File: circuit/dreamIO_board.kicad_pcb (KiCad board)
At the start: 2 copper layers, 60 x 60 mm, 77 parts, among them IC1 TPS61200, P1 BATT, P2 CONN_01X08, P3 CONN_01X08, P4 CONN_01X02, P5 CONN_01X06, P6 gnd_con, P7 CONN_01X03, P9 PixelOut, SW1 SPDT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

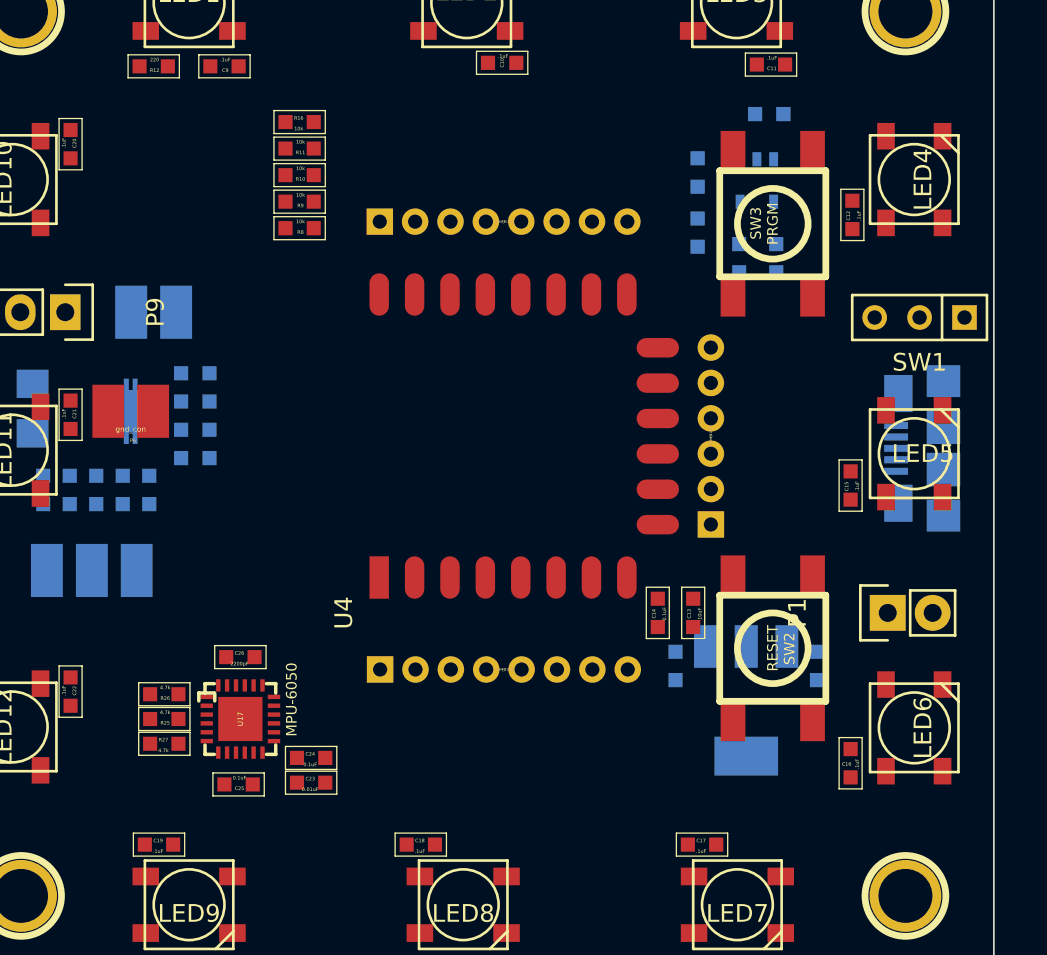
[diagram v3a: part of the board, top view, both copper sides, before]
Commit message: added human input buttons
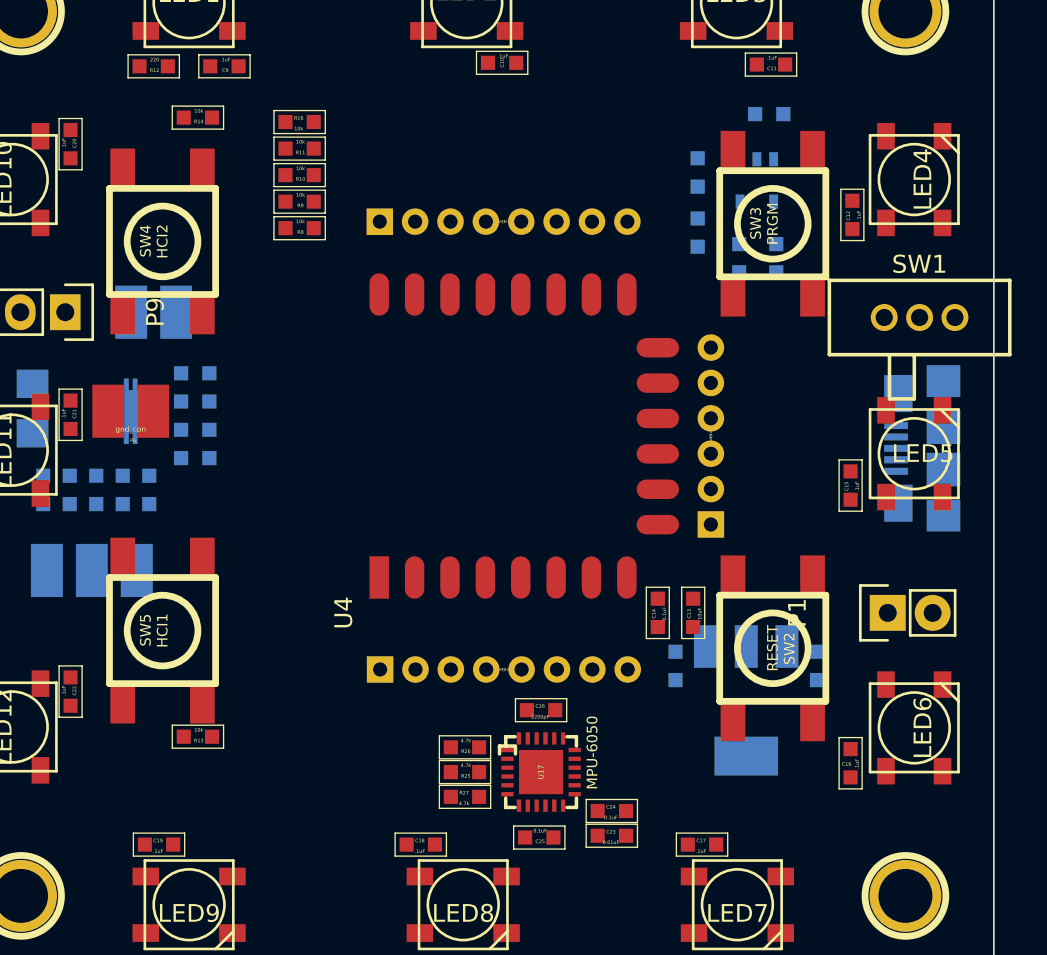
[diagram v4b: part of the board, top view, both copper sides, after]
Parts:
- added R13: 10k, kicad-libraries:0603, F.Cu at (29.3, 59.7)
- added R14: 10k, kicad-libraries:0603, F.Cu at (29.3, 24.7)
- added SW4: HCI2, kicad-libraries:SW_06_SMD, F.Cu at (27.3, 31.7)
- added SW5: HCI1, kicad-libraries:SW_06_SMD, F.Cu at (27.3, 53.7)
- SW1: footprint Buttons_Switches_ThroughHole:SW_Micro_SPST -> dpst:DPST_TE_SSJ12R04
- moved C25 17.3 mm to (48.6, 65.4)
- moved C26 17.3 mm to (48.7, 58.2)
- moved U17 17.3 mm to (48.7, 61.7)
- moved C23 17.3 mm to (52.7, 65.3)
- moved C24 17.3 mm to (52.7, 63.9)
- moved R25 17.3 mm to (44.4, 61.7)
- moved R26 17.3 mm to (44.4, 60.3)
- moved R27 17.3 mm to (44.4, 63.1)
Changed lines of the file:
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@@
 (kicad_pcb (version 4) (host pcbnew 4.0.2-stable)
   (general
-    (links 187)
-    (no_connects 187)
+    (links 199)
+    (no_connects 199)
     (area 14.249999 13.649999 74.350001 73.750001)
     (thickness 1.6)
@@
     (tracks 0)
     (zones 0)
-    (modules 77)
+    (modules 81)
     (nets 53)
   )
@@
   )
   (module kicad-libraries:0603 locked (layer F.Cu)
-    (at 35.7 62.3 180)
+    (at 52.7 65.3 180)
     (attr smd)
     (fp_text reference C23 (at 0.05 0.225 180) (layer F.SilkS)
@@
   )
   (module kicad-libraries:0603 (layer F.Cu)
-    (at 35.7 60.9 180)
+    (at 52.7 63.9 180)
     (attr smd)
     (fp_text reference C24 (at 0.05 0.225 180) (layer F.SilkS)
@@
   )
   (module kicad-libraries:0603 locked (layer F.Cu)
-    (at 31.6 62.4)
+    (at 48.6 65.4)
     (attr smd)
     (fp_text reference C25 (at 0.05 0.225) (layer F.SilkS)
@@
   )
   (module kicad-libraries:0603 locked (layer F.Cu)
-    (at 31.7 55.2 180)
+    (at 48.7 58.2 180)
     (attr smd)
     (fp_text reference C26 (at 0.05 0.225 180) (layer F.SilkS)
@@
   )
   (module kicad-libraries:0603 locked (layer F.Cu)
-    (at 27.4 58.7)
+    (at 44.4 61.7)
     (attr smd)
     (fp_text reference R25 (at 0.05 0.225) (layer F.SilkS)
@@
   )
   (module kicad-libraries:0603 locked (layer F.Cu)
-    (at 27.4 57.3)
+    (at 44.4 60.3)
     (attr smd)
     (fp_text reference R26 (at 0.05 0.225) (layer F.SilkS)
@@
   )
   (module kicad-libraries:0603 locked (layer F.Cu)
-    (at 27.4 60.1 180)
+    (at 44.4 63.1 180)
     (attr smd)
     (fp_text reference R27 (at 0.05 0.225 180) (layer F.SilkS)
@@
     (pad 2 smd rect (at 0.8001 0 180) (size 0.8001 0.8001) (layers F.Cu F.Paste F.Mask)
       (net 2 GND))
-  )
-  (module Buttons_Switches_ThroughHole:SW_Micro_SPST (layer F.Cu)
-    (at 70.1 36 180)
-    (tags "Switch Micro SPST")
-    (fp_text reference SW1 (at 0 -2.54 180) (layer F.SilkS)
-      (effects (font (size 1 1) (thickness 0.15)))
-    )
-    (fp_text value SPDT (at 0.025 2.45 180) (layer F.Fab)
-      (effects (font (size 1 1) (thickness 0.15)))
-    )
-    (fp_line (start -3.81 1.27) (end -3.81 -1.27) (layer F.SilkS) (width 0.15))
-    (fp_line (start -3.81 -1.27) (end 3.81 -1.27) (layer F.SilkS) (width 0.15))
-    (fp_line (start 3.81 -1.27) (end 3.81 1.27) (layer F.SilkS) (width 0.15))
-    (fp_line (start 3.81 1.27) (end -3.81 1.27) (layer F.SilkS) (width 0.15))
-    (fp_line (start -1.27 -1.27) (end -1.27 1.27) (layer F.SilkS) (width 0.15))
-    (pad 1 thru_hole rect (at -2.54 0 180) (size 1.397 1.397) (drill 0.8128) (layers *.Cu *.Mask F.SilkS)
-      (net 4 "Net-(C3-Pad1)"))
-    (pad 2 thru_hole circle (at 0 0 180) (size 1.397 1.397) (drill 0.8128) (layers *.Cu *.Mask F.SilkS)
-      (net 3 +BATT))
-    (pad 3 thru_hole circle (at 2.54 0 180) (size 1.397 1.397) (drill 0.8128) (layers *.Cu *.Mask F.SilkS))
-    (model Buttons_Switches_ThroughHole.3dshapes/SW_Micro_SPST.wrl
-      (at (xyz 0 0 0))
-      (scale (xyz 0.33 0.33 0.33))
-      (rotate (xyz 0 0 0))
-    )
   )
   (module kicad-libraries:SOT23-5 (layer B.Cu)
@@
   )
   (module kicad-libraries:QFN-24-4x4-EP locked (layer F.Cu)
-    (at 31.7 58.7 270)
+    (at 48.7 61.7 270)
     (fp_text reference U17 (at 0 0 270) (layer F.SilkS)
       (effects (font (size 0.29972 0.29972) (thickness 0.06096)))
@@
     (pad 1 thru_hole circle (at 0 0) (size 4.064 4.064) (drill 3.048) (layers *.Cu *.Mask F.SilkS))
   )
+  (module kicad-libraries:0603 (layer F.Cu)
+    (at 29.3 59.7)
+    (attr smd)
+    (fp_text reference R13 (at 0.05 0.225) (layer F.SilkS)
+      (effects (font (size 0.2 0.2) (thickness 0.05)))
+    )
+    (fp_text value 10k (at 0.05 -0.375) (layer F.SilkS)
+      (effects (font (size 0.2 0.2) (thickness 0.05)))
+    )
+    (fp_line (start -1.45034 -0.65024) (end 1.45034 -0.65024) (layer F.SilkS) (width 0.001))
+    (fp_line (start 1.45034 -0.65024) (end 1.45034 0.65024) (layer F.SilkS) (width 0.001))
+    (fp_line (start 1.45034 0.65024) (end -1.45034 0.65024) (layer F.SilkS) (width 0.001))
+    (fp_line (start -1.45034 0.65024) (end -1.45034 -0.65024) (layer F.SilkS) (width 0.001))
+    (pad 1 smd rect (at -0.8001 0) (size 0.8001 0.8001) (layers F.Cu F.Paste F.Mask)
+      (net 2 GND))
+    (pad 2 smd rect (at 0.8001 0) (size 0.8001 0.8001) (layers F.Cu F.Paste F.Mask)
+      (net 9 +3V3))
+  )
+  (module kicad-libraries:0603 (layer F.Cu)
+    (at 29.3 24.7)
+    (attr smd)
+    (fp_text reference R14 (at 0.05 0.225) (layer F.SilkS)
+      (effects (font (size 0.2 0.2) (thickness 0.05)))
+    )
+    (fp_text value 10k (at 0.05 -0.375) (layer F.SilkS)
+      (effects (font (size 0.2 0.2) (thickness 0.05)))
+    )
+    (fp_line (start -1.45034 -0.65024) (end 1.45034 -0.65024) (layer F.SilkS) (width 0.001))
+    (fp_line (start 1.45034 -0.65024) (end 1.45034 0.65024) (layer F.SilkS) (width 0.001))
+    (fp_line (start 1.45034 0.65024) (end -1.45034 0.65024) (layer F.SilkS) (width 0.001))
+    (fp_line (start -1.45034 0.65024) (end -1.45034 -0.65024) (layer F.SilkS) (width 0.001))
+    (pad 1 smd rect (at -0.8001 0) (size 0.8001 0.8001) (layers F.Cu F.Paste F.Mask)
+      (net 2 GND))
+    (pad 2 smd rect (at 0.8001 0) (size 0.8001 0.8001) (layers F.Cu F.Paste F.Mask)
+      (net 9 +3V3))
+  )
+  (module dpst:DPST_TE_SSJ12R04 (layer F.Cu)
+    (at 70.1 36 180)
+    (fp_text reference SW1 (at 0 3 180) (layer F.SilkS)
+      (effects (font (size 1.016 1.016) (thickness 0.1524)))
+    )
+    (fp_text value SPDT (at 0 -5.4 180) (layer F.SilkS) hide
+      (effects (font (size 1.016 1.016) (thickness 0.1524)))
+    )
+    (fp_line (start 1.69926 -2.10058) (end 1.69926 -4.59994) (layer F.SilkS) (width 0.20066))
+    (fp_line (start 1.69926 -4.59994) (end 0.29972 -4.59994) (layer F.SilkS) (width 0.20066))
+    (fp_line (start 0.29972 -4.59994) (end 0.29972 -2.10058) (layer F.SilkS) (width 0.20066))
+    (fp_line (start 5.10032 -2.10058) (end -5.10032 -2.10058) (layer F.SilkS) (width 0.20066))
+    (fp_line (start -5.10032 -2.10058) (end -5.10032 2.10058) (layer F.SilkS) (width 0.20066))
+    (fp_line (start -5.10032 2.10058) (end 5.10032 2.10058) (layer F.SilkS) (width 0.20066))
+    (fp_line (start 5.10032 2.10058) (end 5.10032 -2.10058) (layer F.SilkS) (width 0.20066))
+    (pad 1 thru_hole circle (at -1.99898 0 180) (size 1.524 1.524) (drill 0.97028) (layers *.Cu *.Mask F.SilkS)
+      (net 4 "Net-(C3-Pad1)"))
+    (pad 2 thru_hole circle (at 0 0 180) (size 1.524 1.524) (drill 0.97028) (layers *.Cu *.Mask F.SilkS)
+      (net 3 +BATT))
+    (pad 3 thru_hole circle (at 1.99898 0 180) (size 1.524 1.524) (drill 0.97028) (layers *.Cu *.Mask F.SilkS))
+    (model 3D/Switches/TE_SSJ12R04.wrl
+      (at (xyz 0 0 0))
+      (scale (xyz 0.3937 0.3937 0.3937))
+      (rotate (xyz 0 0 0))
+    )
+  )
+  (module kicad-libraries:SW_06_SMD (layer F.Cu)
+    (at 27.3 31.7 90)
+    (fp_text reference SW4 (at 0.0254 -0.94996 90) (layer F.SilkS)
+      (effects (font (size 0.59944 0.59944) (thickness 0.09906)))
+    )
+    (fp_text value HCI2 (at 0 0 90) (layer F.SilkS)
+      (effects (font (size 0.59944 0.59944) (thickness 0.09906)))
+    )
+    (fp_circle (center 0 0) (end 1.99898 0) (layer F.SilkS) (width 0.381))
+    (fp_line (start -2.99974 -2.99974) (end 2.99974 -2.99974) (layer F.SilkS) (width 0.381))
+    (fp_line (start 2.99974 -2.99974) (end 2.99974 2.99974) (layer F.SilkS) (width 0.381))
+    (fp_line (start 2.99974 2.99974) (end -2.99974 2.99974) (layer F.SilkS) (width 0.381))
+    (fp_line (start -2.99974 2.99974) (end -2.99974 -2.99974) (layer F.SilkS) (width 0.381))
+    (pad 1 smd rect (at -4.20116 -2.25044 90) (size 2.10058 1.39954) (layers F.Cu F.Paste F.Mask)
+      (net 35 GPIO16))
+    (pad 2 smd rect (at -4.20116 2.25044 90) (size 2.10058 1.39954) (layers F.Cu F.Paste F.Mask)
+      (net 9 +3V3))
+    (pad 2 smd rect (at 4.20116 2.25044 90) (size 2.10058 1.39954) (layers F.Cu F.Paste F.Mask)
+      (net 9 +3V3))
+    (pad 1 smd rect (at 4.20116 -2.25044 90) (size 2.10058 1.39954) (layers F.Cu F.Paste F.Mask)
+      (net 35 GPIO16))
+  )
+  (module kicad-libraries:SW_06_SMD (layer F.Cu)
+    (at 27.3 53.7 90)
+    (fp_text reference SW5 (at 0.0254 -0.94996 90) (layer F.SilkS)
+      (effects (font (size 0.59944 0.59944) (thickness 0.09906)))
+    )
+    (fp_text value HCI1 (at 0 0 90) (layer F.SilkS)
+      (effects (font (size 0.59944 0.59944) (thickness 0.09906)))
+    )
+    (fp_circle (center 0 0) (end 1.99898 0) (layer F.SilkS) (width 0.381))
+    (fp_line (start -2.99974 -2.99974) (end 2.99974 -2.99974) (layer F.SilkS) (width 0.381))
+    (fp_line (start 2.99974 -2.99974) (end 2.99974 2.99974) (layer F.SilkS) (width 0.381))
+    (fp_line (start 2.99974 2.99974) (end -2.99974 2.99974) (layer F.SilkS) (width 0.381))
+    (fp_line (start -2.99974 2.99974) (end -2.99974 -2.99974) (layer F.SilkS) (width 0.381))
+    (pad 1 smd rect (at -4.20116 -2.25044 90) (size 2.10058 1.39954) (layers F.Cu F.Paste F.Mask)
+      (net 37 GPIO14))
+    (pad 2 smd rect (at -4.20116 2.25044 90) (size 2.10058 1.39954) (layers F.Cu F.Paste F.Mask)
+      (net 9 +3V3))
+    (pad 2 smd rect (at 4.20116 2.25044 90) (size 2.10058 1.39954) (layers F.Cu F.Paste F.Mask)
+      (net 9 +3V3))
+    (pad 1 smd rect (at 4.20116 -2.25044 90) (size 2.10058 1.39954) (layers F.Cu F.Paste F.Mask)
+      (net 37 GPIO14))
+  )
   (gr_line (start 14.3 13.7) (end 24.3 13.7) (angle 90) (layer Cmts.User) (width 0.2))

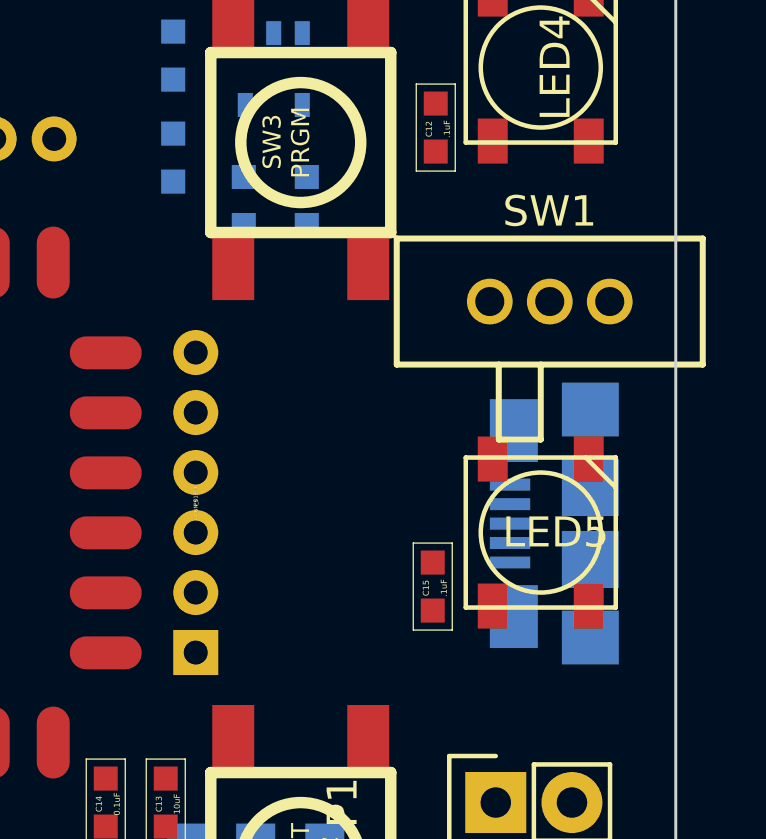
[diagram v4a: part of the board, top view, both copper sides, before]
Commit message: moved the on off switch
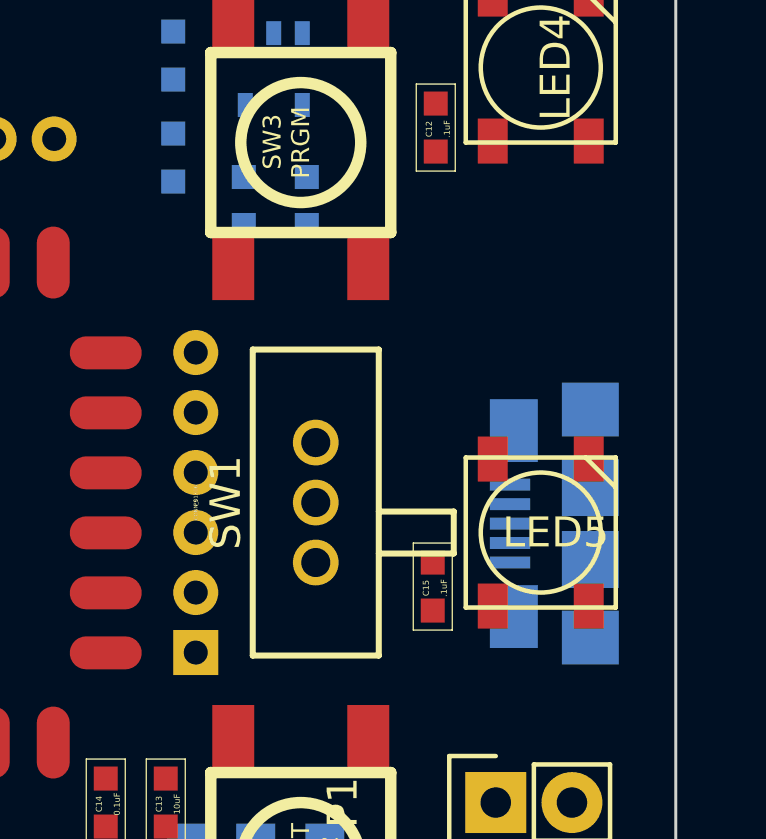
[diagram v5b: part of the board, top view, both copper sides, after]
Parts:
- moved SW1 10.3 mm to (62.3, 42.7), turned to 270 degrees
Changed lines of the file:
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@@
     (links 199)
     (no_connects 199)
-    (area 14.249999 13.649999 74.350001 73.750001)
+    (area 14.199999 13.599999 75.500651 73.750001)
     (thickness 1.6)
     (drawings 8)
@@
   )
   (module dpst:DPST_TE_SSJ12R04 (layer F.Cu)
-    (at 70.1 36 180)
-    (fp_text reference SW1 (at 0 3 180) (layer F.SilkS)
+    (at 62.3 42.7 270)
+    (fp_text reference SW1 (at 0 3 270) (layer F.SilkS)
       (effects (font (size 1.016 1.016) (thickness 0.1524)))
     )
-    (fp_text value SPDT (at 0 -5.4 180) (layer F.SilkS) hide
+    (fp_text value SPDT (at 0 -5.4 270) (layer F.SilkS) hide
       (effects (font (size 1.016 1.016) (thickness 0.1524)))
     )
@@
     (fp_line (start -5.10032 2.10058) (end 5.10032 2.10058) (layer F.SilkS) (width 0.20066))
     (fp_line (start 5.10032 2.10058) (end 5.10032 -2.10058) (layer F.SilkS) (width 0.20066))
-    (pad 1 thru_hole circle (at -1.99898 0 180) (size 1.524 1.524) (drill 0.97028) (layers *.Cu *.Mask F.SilkS)
+    (pad 1 thru_hole circle (at -1.99898 0 270) (size 1.524 1.524) (drill 0.97028) (layers *.Cu *.Mask F.SilkS)
       (net 4 "Net-(C3-Pad1)"))
-    (pad 2 thru_hole circle (at 0 0 180) (size 1.524 1.524) (drill 0.97028) (layers *.Cu *.Mask F.SilkS)
+    (pad 2 thru_hole circle (at 0 0 270) (size 1.524 1.524) (drill 0.97028) (layers *.Cu *.Mask F.SilkS)
       (net 3 +BATT))
-    (pad 3 thru_hole circle (at 1.99898 0 180) (size 1.524 1.524) (drill 0.97028) (layers *.Cu *.Mask F.SilkS))
+    (pad 3 thru_hole circle (at 1.99898 0 270) (size 1.524 1.524) (drill 0.97028) (layers *.Cu *.Mask F.SilkS))
     (model 3D/Switches/TE_SSJ12R04.wrl
       (at (xyz 0 0 0))

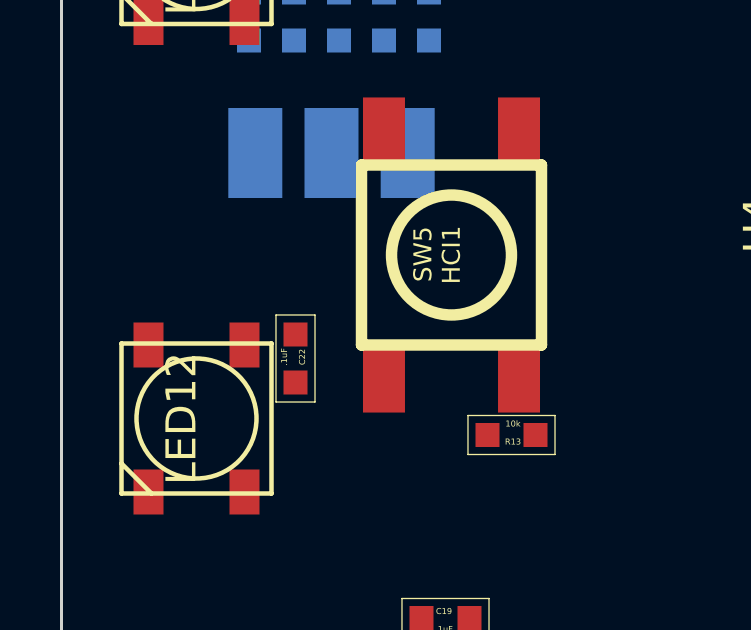
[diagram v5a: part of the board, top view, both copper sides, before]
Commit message: realized the cascaded regulators might not be necessary since the output of the Neopixels at 3.3v is quite bright. While 5V would be brighter, it may not always be necessary to buy the extra parts
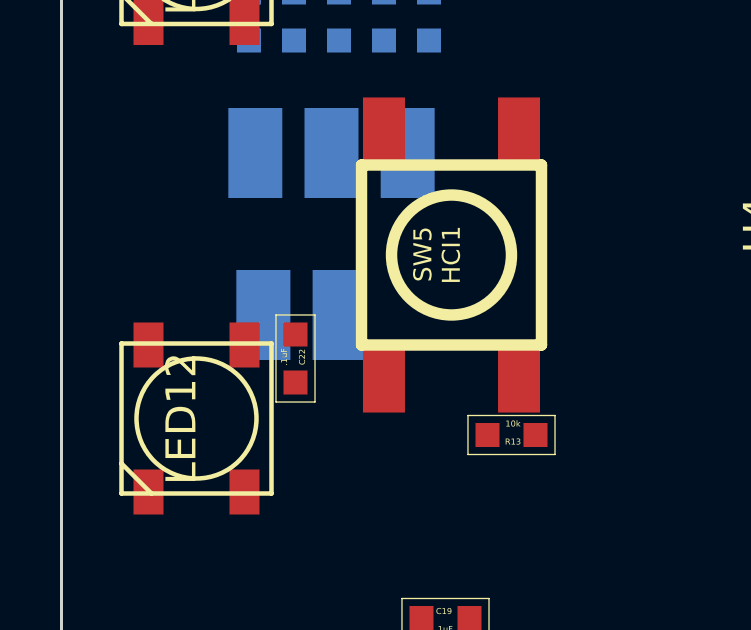
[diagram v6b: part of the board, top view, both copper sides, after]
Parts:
- added P8: NO_CASCADE, _connectors:_Solder_Pad2.54_2, B.Cu at (22.3, 55.7)
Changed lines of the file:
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@@
 (kicad_pcb (version 4) (host pcbnew 4.0.2-stable)
   (general
-    (links 199)
-    (no_connects 199)
-    (area 14.199999 13.599999 75.500651 73.750001)
+    (links 201)
+    (no_connects 201)
+    (area 14.249999 13.649999 74.350001 73.750001)
     (thickness 1.6)
     (drawings 8)
     (tracks 0)
     (zones 0)
-    (modules 81)
+    (modules 82)
     (nets 53)
   )
@@
       (net 37 GPIO14))
   )
+  (module _connectors:_Solder_Pad2.54_2 (layer B.Cu)
+    (at 22.3 55.7)
+    (fp_text reference P8 (at -0.127 1.651) (layer B.SilkS)
+      (effects (font (size 0.2 0.2) (thickness 0.05)) (justify mirror))
+    )
+    (fp_text value NO_CASCADE (at 0 1.016) (layer B.SilkS)
+      (effects (font (size 0.3 0.3) (thickness 0.075)) (justify mirror))
+    )
+    (pad 1 smd rect (at -1.27 0) (size 1.8 3) (layers B.Cu B.Paste B.Mask)
+      (net 7 VCC) (clearance 0.508))
+    (pad 2 smd rect (at 1.27 0) (size 1.8 3) (layers B.Cu B.Paste B.Mask)
+      (net 9 +3V3) (clearance 0.508))
+  )
   (gr_line (start 14.3 13.7) (end 24.3 13.7) (angle 90) (layer Cmts.User) (width 0.2))
